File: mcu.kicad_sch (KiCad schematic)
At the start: 29 parts

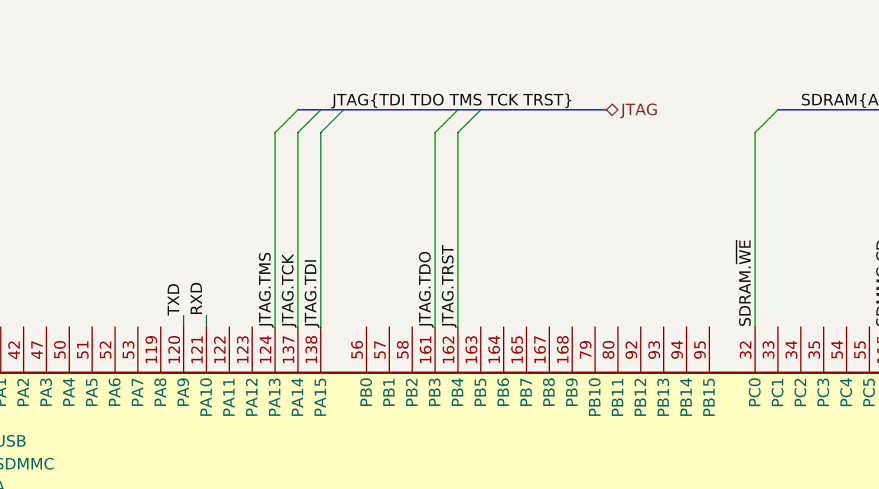
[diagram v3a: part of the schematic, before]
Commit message: Add MCU USB
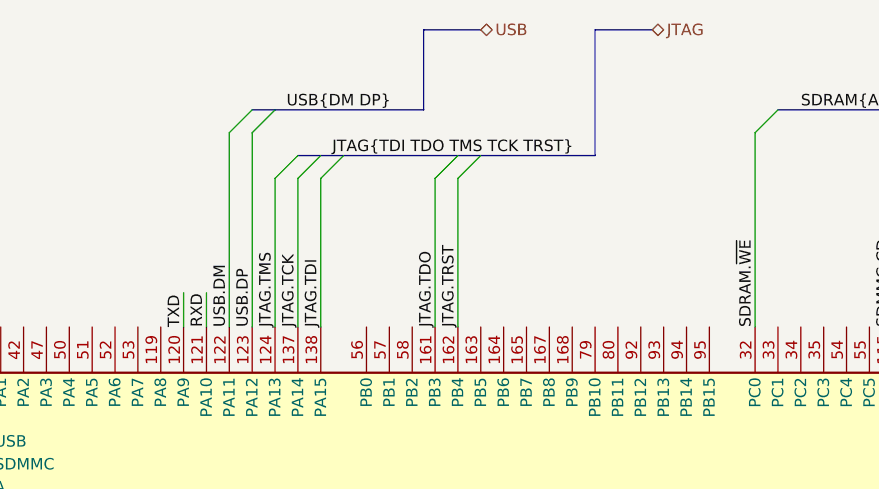
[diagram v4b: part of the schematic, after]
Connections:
- net USB.DM: now reaches U?.122 (PA11)
- net USB.DP: now reaches U?.123 (PA12)
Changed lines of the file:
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@@
   )
   (no_connect (at 139.7 166.37))
+  (bus_entry (at 82.55 26.67) (size -2.54 2.54)
+    (stroke (width 0) (type default) (color 0 0 0 0))
+  )
   (bus_entry (at 260.35 144.78) (size 2.54 2.54)
     (stroke (width 0) (type default) (color 0 0 0 0))
@@
     (stroke (width 0) (type default) (color 0 0 0 0))
   )
-  (bus_entry (at 105.41 26.67) (size -2.54 2.54)
+  (bus_entry (at 105.41 31.75) (size -2.54 2.54)
     (stroke (width 0) (type default) (color 0 0 0 0))
   )
@@
     (stroke (width 0) (type default) (color 0 0 0 0))
   )
-  (bus_entry (at 107.95 26.67) (size -2.54 2.54)
+  (bus_entry (at 107.95 31.75) (size -2.54 2.54)
     (stroke (width 0) (type default) (color 0 0 0 0))
   )
@@
     (stroke (width 0) (type default) (color 0 0 0 0))
   )
-  (bus_entry (at 90.17 26.67) (size -2.54 2.54)
+  (bus_entry (at 90.17 31.75) (size -2.54 2.54)
     (stroke (width 0) (type default) (color 0 0 0 0))
   )
@@
     (stroke (width 0) (type default) (color 0 0 0 0))
   )
-  (bus_entry (at 92.71 26.67) (size -2.54 2.54)
+  (bus_entry (at 92.71 31.75) (size -2.54 2.54)
     (stroke (width 0) (type default) (color 0 0 0 0))
   )
@@
     (stroke (width 0) (type default) (color 0 0 0 0))
   )
-  (bus_entry (at 87.63 26.67) (size -2.54 2.54)
+  (bus_entry (at 85.09 26.67) (size -2.54 2.54)
+    (stroke (width 0) (type default) (color 0 0 0 0))
+  )
+  (bus_entry (at 87.63 31.75) (size -2.54 2.54)
     (stroke (width 0) (type default) (color 0 0 0 0))
   )
@@
     (stroke (width 0) (type default) (color 0 0 0 0))
   )
+  (bus (pts (xy 107.95 31.75) (xy 120.65 31.75))
+    (stroke (width 0) (type default) (color 0 0 0 0))
+  )
   (wire (pts (xy 143.51 124.46) (xy 143.51 144.78))
     (stroke (width 0) (type default) (color 0 0 0 0))
@@
     (stroke (width 0) (type default) (color 0 0 0 0))
   )
+  (wire (pts (xy 85.09 34.29) (xy 85.09 50.8))
+    (stroke (width 0) (type default) (color 0 0 0 0))
+  )
   (wire (pts (xy 22.86 73.66) (xy 22.86 68.58))
     (stroke (width 0) (type default) (color 0 0 0 0))
@@
     (stroke (width 0) (type default) (color 0 0 0 0))
   )
+  (bus (pts (xy 127 17.78) (xy 120.65 17.78))
+    (stroke (width 0) (type default) (color 0 0 0 0))
+  )
   (wire (pts (xy 43.18 144.78) (xy 62.23 144.78))
     (stroke (width 0) (type default) (color 0 0 0 0))
@@
     (stroke (width 0) (type default) (color 0 0 0 0))
   )
+  (bus (pts (xy 101.6 26.67) (xy 101.6 17.78))
+    (stroke (width 0) (type default) (color 0 0 0 0))
+  )
+  (bus (pts (xy 85.09 26.67) (xy 101.6 26.67))
+    (stroke (width 0) (type default) (color 0 0 0 0))
+  )
   (wire (pts (xy 41.91 63.5) (xy 41.91 66.04))
     (stroke (width 0) (type default) (color 0 0 0 0))
@@
     (stroke (width 0) (type default) (color 0 0 0 0))
   )
-  (bus (pts (xy 92.71 26.67) (xy 105.41 26.67))
+  (bus (pts (xy 92.71 31.75) (xy 105.41 31.75))
     (stroke (width 0) (type default) (color 0 0 0 0))
   )
@@
     (stroke (width 0) (type default) (color 0 0 0 0))
   )
-  (wire (pts (xy 90.17 29.21) (xy 90.17 50.8))
+  (wire (pts (xy 90.17 34.29) (xy 90.17 50.8))
     (stroke (width 0) (type default) (color 0 0 0 0))
   )
@@
     (stroke (width 0) (type default) (color 0 0 0 0))
   )
-  (bus (pts (xy 87.63 26.67) (xy 90.17 26.67))
+  (bus (pts (xy 87.63 31.75) (xy 90.17 31.75))
     (stroke (width 0) (type default) (color 0 0 0 0))
   )
@@
     (stroke (width 0) (type default) (color 0 0 0 0))
   )
+  (wire (pts (xy 82.55 29.21) (xy 82.55 50.8))
+    (stroke (width 0) (type default) (color 0 0 0 0))
+  )
   (wire (pts (xy 204.47 29.21) (xy 204.47 50.8))
     (stroke (width 0) (type default) (color 0 0 0 0))
@@
     (stroke (width 0) (type default) (color 0 0 0 0))
   )
-  (wire (pts (xy 105.41 29.21) (xy 105.41 50.8))
+  (wire (pts (xy 105.41 34.29) (xy 105.41 50.8))
     (stroke (width 0) (type default) (color 0 0 0 0))
   )
@@
     (stroke (width 0) (type default) (color 0 0 0 0))
   )
+  (wire (pts (xy 80.01 29.21) (xy 80.01 50.8))
+    (stroke (width 0) (type default) (color 0 0 0 0))
+  )
   (wire (pts (xy 138.43 29.21) (xy 138.43 50.8))
     (stroke (width 0) (type default) (color 0 0 0 0))
@@
     (stroke (width 0) (type default) (color 0 0 0 0))
   )
+  (bus (pts (xy 82.55 26.67) (xy 85.09 26.67))
+    (stroke (width 0) (type default) (color 0 0 0 0))
+  )
   (bus (pts (xy 236.22 17.78) (xy 248.92 17.78))
     (stroke (width 0) (type default) (color 0 0 0 0))
@@
     (stroke (width 0) (type default) (color 0 0 0 0))
   )
-  (bus (pts (xy 107.95 26.67) (xy 121.92 26.67))
-    (stroke (width 0) (type default) (color 0 0 0 0))
-  )
   (wire (pts (xy 41.91 76.2) (xy 44.45 76.2))
     (stroke (width 0) (type default) (color 0 0 0 0))
@@
     (stroke (width 0) (type default) (color 0 0 0 0))
   )
+  (bus (pts (xy 101.6 17.78) (xy 107.95 17.78))
+    (stroke (width 0) (type default) (color 0 0 0 0))
+  )
   (wire (pts (xy 242.57 29.21) (xy 242.57 50.8))
     (stroke (width 0) (type default) (color 0 0 0 0))
@@
     (stroke (width 0) (type default) (color 0 0 0 0))
   )
-  (bus (pts (xy 105.41 26.67) (xy 107.95 26.67))
+  (bus (pts (xy 105.41 31.75) (xy 107.95 31.75))
     (stroke (width 0) (type default) (color 0 0 0 0))
   )
@@
     (stroke (width 0) (type default) (color 0 0 0 0))
   )
+  (bus (pts (xy 120.65 17.78) (xy 120.65 31.75))
+    (stroke (width 0) (type default) (color 0 0 0 0))
+  )
   (wire (pts (xy 41.91 101.6) (xy 44.45 101.6))
     (stroke (width 0) (type default) (color 0 0 0 0))
@@
     (stroke (width 0) (type default) (color 0 0 0 0))
   )
+  (wire (pts (xy 74.93 46.99) (xy 74.93 50.8))
+    (stroke (width 0) (type default) (color 0 0 0 0))
+  )
   (wire (pts (xy 274.32 83.82) (xy 274.32 86.36))
     (stroke (width 0) (type default) (color 0 0 0 0))
@@
     (stroke (width 0) (type default) (color 0 0 0 0))
   )
-  (wire (pts (xy 85.09 29.21) (xy 85.09 50.8))
-    (stroke (width 0) (type default) (color 0 0 0 0))
-  )
   (wire (pts (xy 41.91 88.9) (xy 44.45 88.9))
     (stroke (width 0) (type default) (color 0 0 0 0))
@@
     (stroke (width 0) (type default) (color 0 0 0 0))
   )
-  (wire (pts (xy 74.93 49.53) (xy 74.93 50.8))
-    (stroke (width 0) (type default) (color 0 0 0 0))
-  )
   (wire (pts (xy 90.17 173.99) (xy 102.87 173.99))
     (stroke (width 0) (type default) (color 0 0 0 0))
@@
     (stroke (width 0) (type default) (color 0 0 0 0))
   )
-  (wire (pts (xy 102.87 29.21) (xy 102.87 50.8))
+  (wire (pts (xy 102.87 34.29) (xy 102.87 50.8))
     (stroke (width 0) (type default) (color 0 0 0 0))
   )
@@
     (stroke (width 0) (type default) (color 0 0 0 0))
   )
-  (wire (pts (xy 77.47 49.53) (xy 77.47 50.8))
-    (stroke (width 0) (type default) (color 0 0 0 0))
-  )
   (bus (pts (xy 250.19 26.67) (xy 252.73 26.67))
     (stroke (width 0) (type default) (color 0 0 0 0))
@@
     (stroke (width 0) (type default) (color 0 0 0 0))
   )
-  (bus (pts (xy 90.17 26.67) (xy 92.71 26.67))
+  (bus (pts (xy 90.17 31.75) (xy 92.71 31.75))
     (stroke (width 0) (type default) (color 0 0 0 0))
   )
@@
     (stroke (width 0) (type default) (color 0 0 0 0))
   )
+  (wire (pts (xy 77.47 46.99) (xy 77.47 50.8))
+    (stroke (width 0) (type default) (color 0 0 0 0))
+  )
   (wire (pts (xy 146.05 124.46) (xy 146.05 144.78))
     (stroke (width 0) (type default) (color 0 0 0 0))
@@
     (stroke (width 0) (type default) (color 0 0 0 0))
   )
-  (wire (pts (xy 87.63 29.21) (xy 87.63 50.8))
+  (wire (pts (xy 87.63 34.29) (xy 87.63 50.8))
     (stroke (width 0) (type default) (color 0 0 0 0))
   )
@@
     (effects (font (size 1.27 1.27)) (justify left bottom))
   )
-  (label "RXD" (at 77.47 49.53 90)
+  (label "USB.DP" (at 82.55 50.8 90)
+    (effects (font (size 1.27 1.27)) (justify left bottom))
+  )
+  (label "RXD" (at 77.47 50.8 90)
     (effects (font (size 1.27 1.27)) (justify left bottom))
   )
@@
     (effects (font (size 1.27 1.27)) (justify left bottom))
   )
+  (label "USB.DM" (at 80.01 50.8 90)
+    (effects (font (size 1.27 1.27)) (justify left bottom))
+  )
   (label "SDRAM.D1" (at 219.71 50.8 90)
     (effects (font (size 1.27 1.27)) (justify left bottom))
@@
     (effects (font (size 1.27 1.27)) (justify right bottom))
   )
-  (label "JTAG{TDI TDO TMS TCK TRST}" (at 91.44 26.67 0)
+  (label "JTAG{TDI TDO TMS TCK TRST}" (at 91.44 31.75 0)
     (effects (font (size 1.27 1.27)) (justify left bottom))
   )
@@
   )
   (label "SDRAM.D15" (at 207.01 50.8 90)
+    (effects (font (size 1.27 1.27)) (justify left bottom))
+  )
+  (label "USB{DM DP}" (at 86.36 26.67 0)
     (effects (font (size 1.27 1.27)) (justify left bottom))
   )
@@
     (effects (font (size 1.27 1.27)) (justify left bottom))
   )
-  (label "TXD" (at 74.93 49.53 90)
+  (label "TXD" (at 74.93 50.8 90)
     (effects (font (size 1.27 1.27)) (justify left bottom))
   )
@@
     (effects (font (size 1.27 1.27)) (justify right bottom))
   )
-  (hierarchical_label "JTAG" (shape bidirectional) (at 121.92 26.67 0)
+  (hierarchical_label "JTAG" (shape bidirectional) (at 127 17.78 0)
     (effects (font (size 1.27 1.27)) (justify left))
   )
@@
     (effects (font (size 1.27 1.27)) (justify right))
   )
+  (hierarchical_label "USB" (shape bidirectional) (at 107.95 17.78 0)
+    (effects (font (size 1.27 1.27)) (justify left))
+  )
   (hierarchical_label "~{RESET}" (shape bidirectional) (at 53.34 151.13 0)

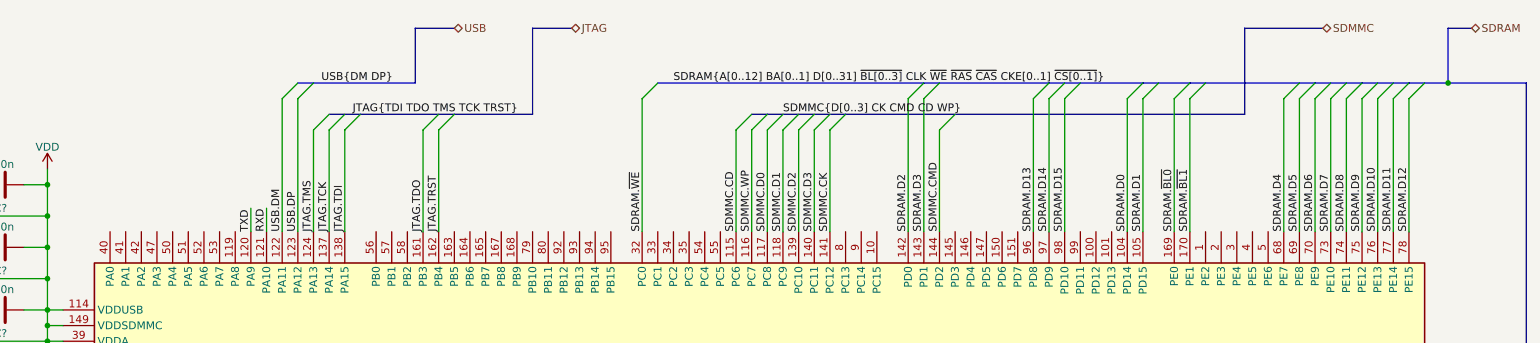
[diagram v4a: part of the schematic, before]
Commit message: Add Ethernet interface.
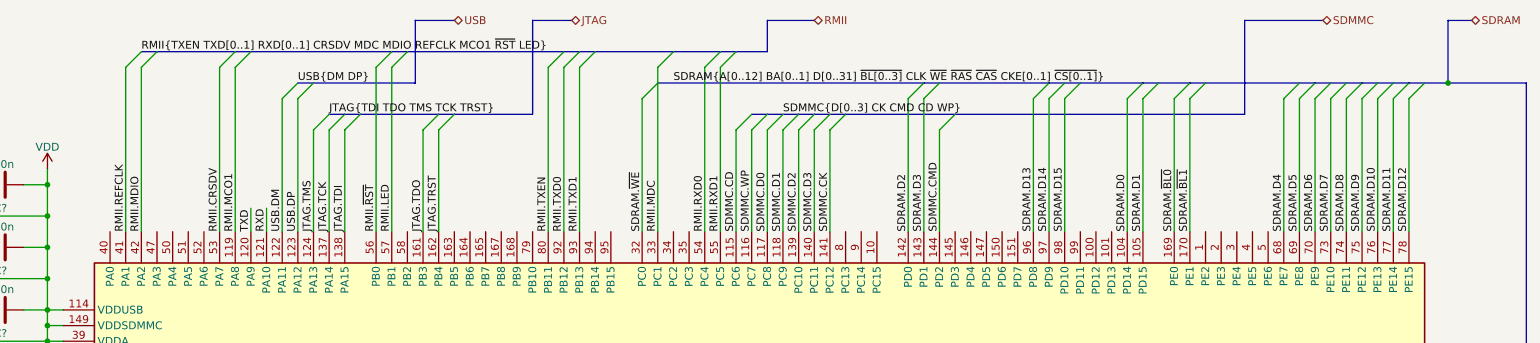
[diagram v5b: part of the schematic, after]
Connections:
- net RMII.MCO1: now reaches U?.119 (PA8)
- net RMII.MDC: now reaches U?.33 (PC1)
- net RMII.REFCLK: now reaches U?.41 (PA1)
- net RMII.MDIO: now reaches U?.42 (PA2)
- net RMII.CRSDV: now reaches U?.53 (PA7)
- net RMII.RXD0: now reaches U?.54 (PC4)
- net RMII.RXD1: now reaches U?.55 (PC5)
- net RMII.~{RST}: now reaches U?.56 (PB0)
- net RMII.LED: now reaches U?.57 (PB1)
- net RMII.TXEN: now reaches U?.80 (PB11)
- net RMII.TXD0: now reaches U?.92 (PB12)
- net RMII.TXD1: now reaches U?.93 (PB13)

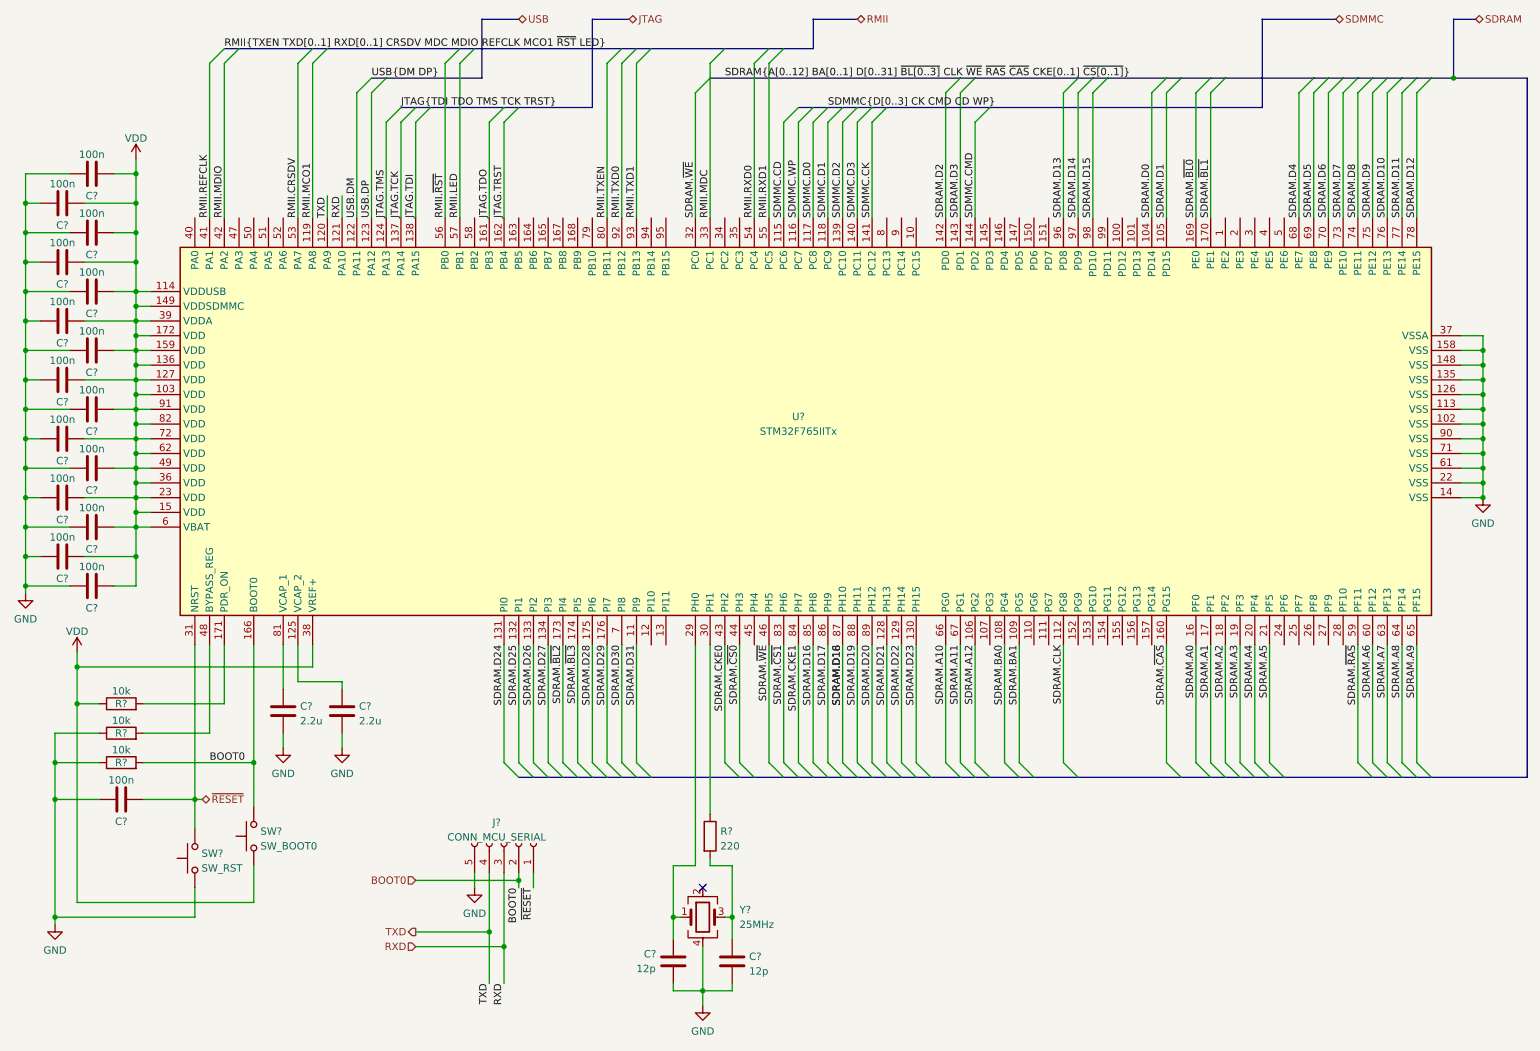
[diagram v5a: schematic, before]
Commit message: Capacitor part assignment
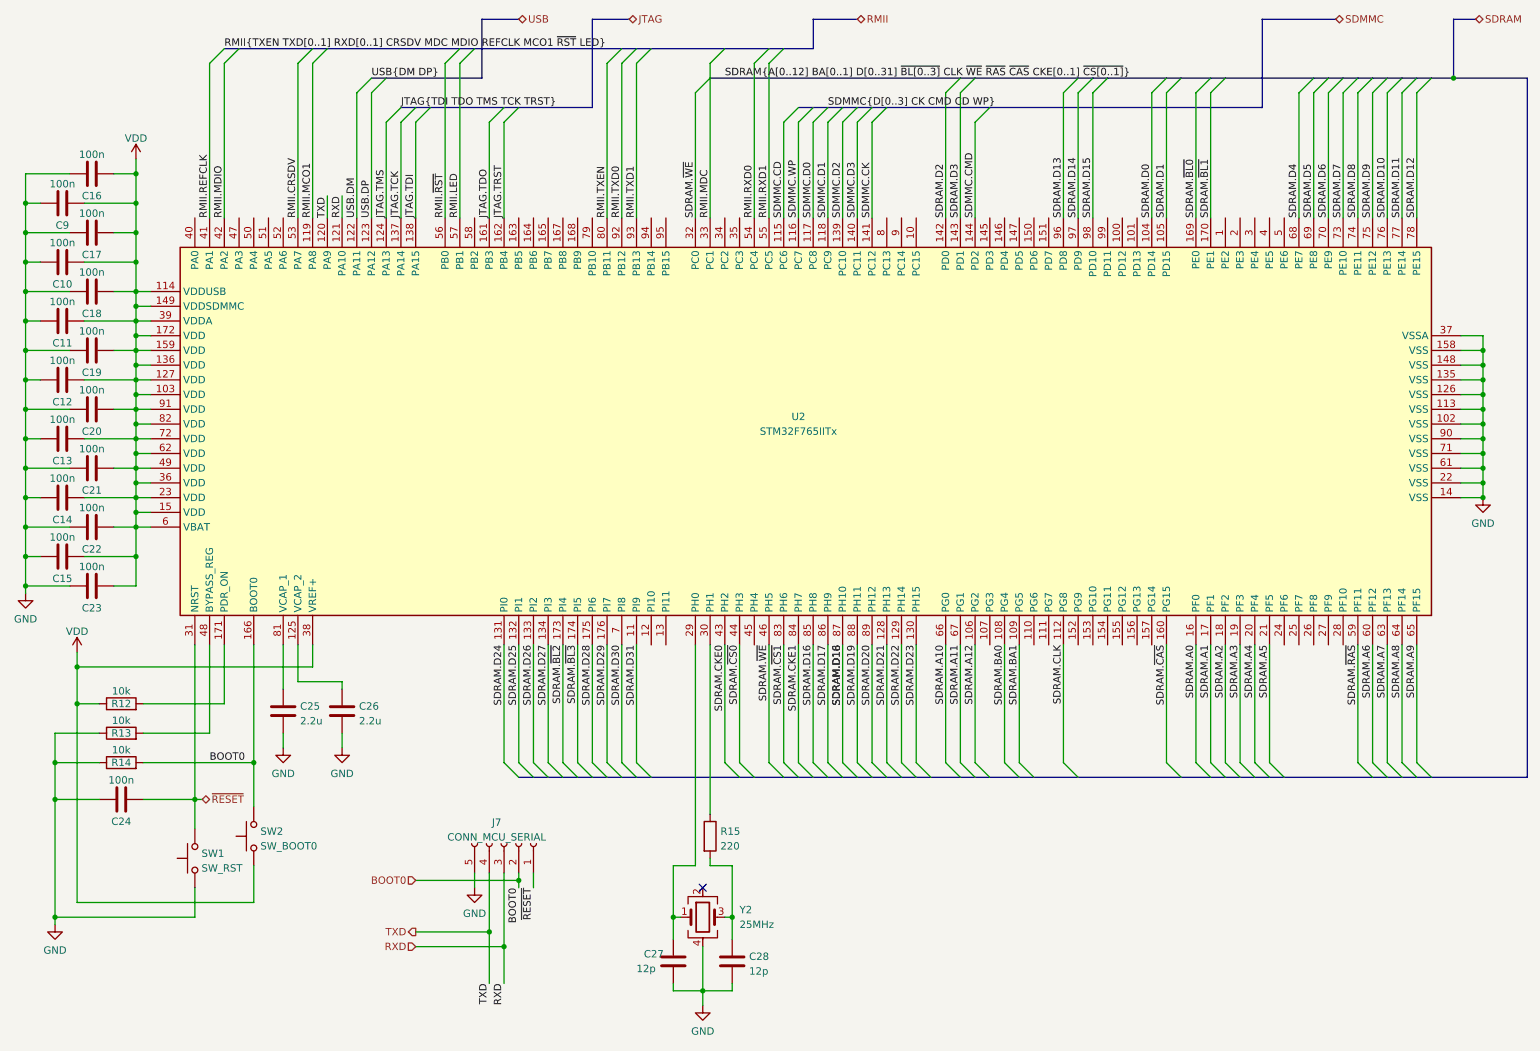
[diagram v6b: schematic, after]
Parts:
- C10, C11, C12, C13, C14, C15, C16, C17, C18, C19, C20, C21, C22, C23, C24, C27, C28, C9: renamed from C?; footprint (none) -> Capacitor_SMD:C_0603_1608Metric_Pad1.08x0.95mm_HandSolder
- C25, C26: renamed from C?; footprint (none) -> Capacitor_SMD:C_0805_2012Metric_Pad1.18x1.45mm_HandSolder
- gave numbers to parts that had none: 9
